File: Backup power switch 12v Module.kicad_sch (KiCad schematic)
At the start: 20 parts, among them J1 BAT IN, J2 PWR IN, J3 LOAD PWR OUT, K1 SANYOU_SRD_Form_C, Q3 BC817, U1 LM393

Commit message: DRC check
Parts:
- D7: footprint Package_TO_SOT_THT:TO-247-3_Vertical -> PCM_Package_TO_SOT_THT_AKL_OneLayer:TO-220-3_Staggered_Vertical
- K1: value SANYOU_SRD_Form_C -> SRD-12VDC-SL-C
- U1: footprint Package_SO:SOP-8_3.76x4.96mm_P1.27mm -> Package_DIP:DIP-8_W7.62mm
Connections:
- net COMMON OUT 12 +: no longer C5.1, D2.1 (K), D7.2 (K), K1.5, U1.8 (V+)
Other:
- note added: "Backup batary switch with charger, sensors and ESP controller"
- note added: "Comparator LM393"
- note added: "Switchng module"
- note removed: "Bat > PWR Signal High"
- note removed: "PWR > BAT Signal Low"
- note removed: "Pin3 < Pin2 Signal High"
- note removed: "Pin3 > Pin2 Signal High"
- note removed: "Зарядка батареи с двумя сенсорами тока"
- note removed: "Компаратор LM393"
- moved on the sheet: C5, D6, D7, J1, J2, J3, R13, R2, R3, RV1, TP1, TP2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

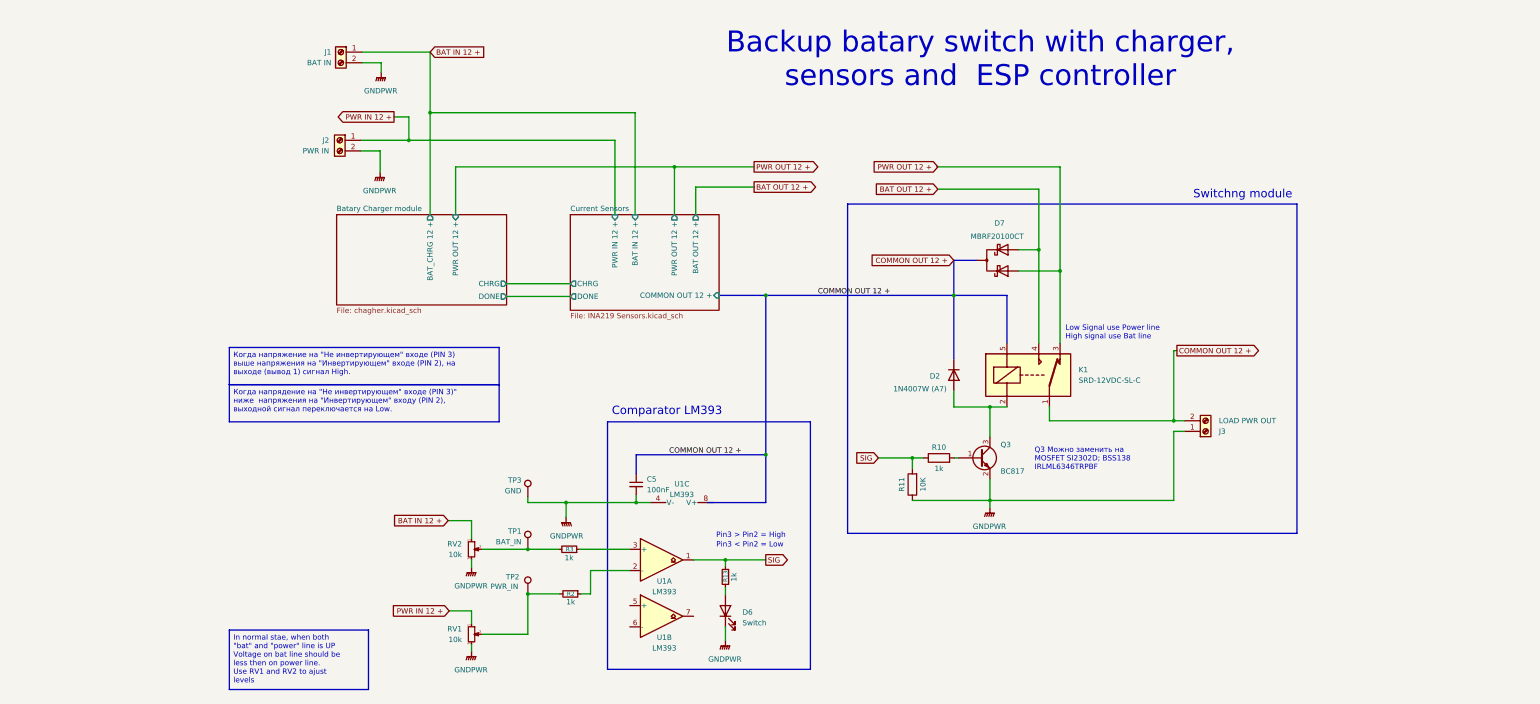
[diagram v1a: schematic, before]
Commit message: Add bat input stabilizer
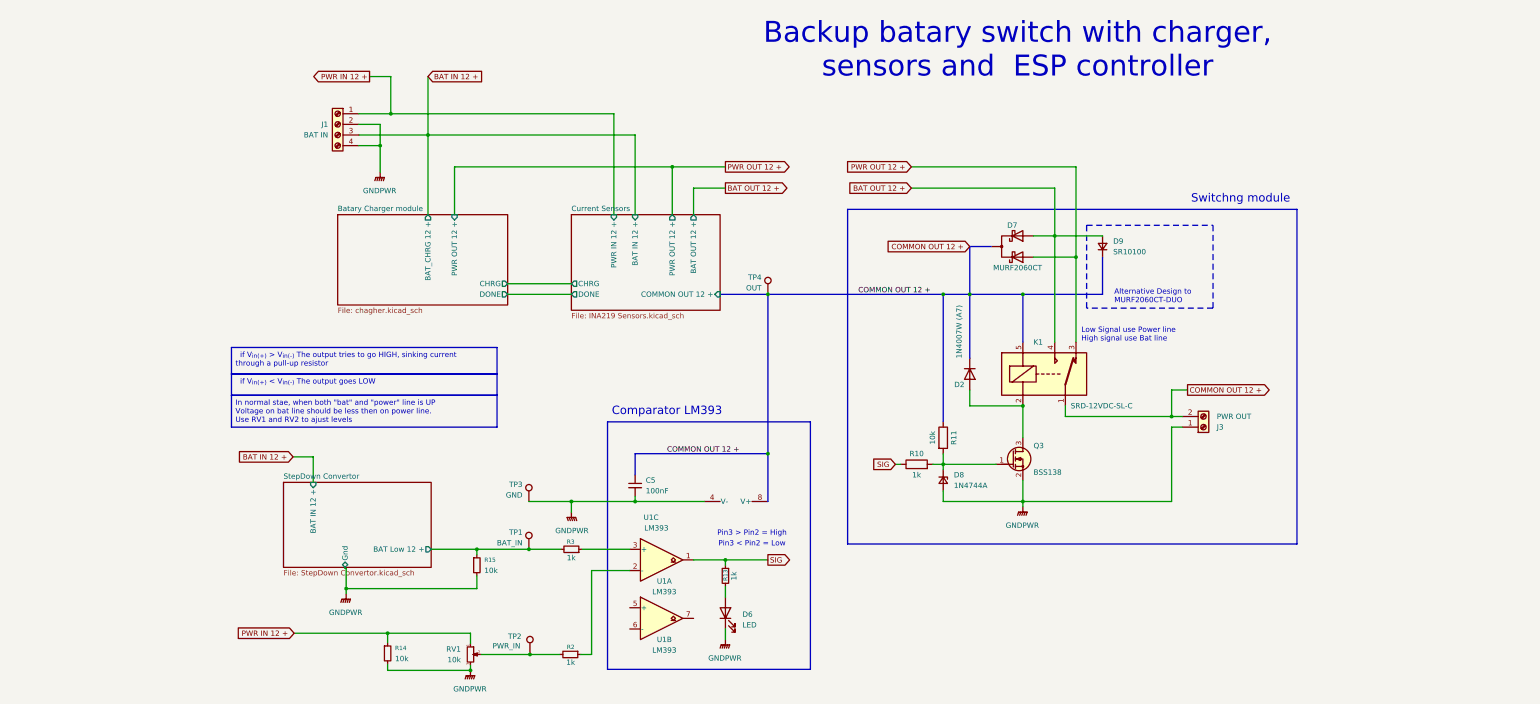
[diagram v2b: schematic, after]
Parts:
- removed J2: PWR IN, TerminalBlock_Local:ScrewTerminal_KF7.62_2P, symbol Connector:Screw_Terminal_01x02
- removed RV2: 10k, Potentiometer_THT:Potentiometer_Bourns_3296W_Vertical, symbol Device:R_Potentiometer_Small
- added D8: 1N4744A, Diode_THT:D_DO-41_SOD81_P7.62mm_Horizontal, symbol Device:D_Zener_Small
- added D9: SR10100, symbol Device:D_Small
- added R14, R15: 10k, PCM_Resistor_SMD_AKL:R_0805_2012Metric_Pad1.15x1.40mm_HandSolder, symbol Device:R_Small
- added TP4: OUT, TestPoint:TestPoint_Loop_D2.50mm_Drill1.85mm, symbol Connector:TestPoint
- D6: value Switch -> LED; descr (none) -> ON when level UP
- D7: value MBRF20100CT -> MURF2060CT
- J1: footprint TerminalBlock_Local:ScrewTerminal_KF7.62_2P -> TerminalBlock_Local:ScrewTerminal_KF7.62_4P; symbol Connector:Screw_Terminal_01x02 -> Connector:Screw_Terminal_01x04
- J3: value LOAD PWR OUT -> PWR OUT
- Q3: value BC817 -> BSS138; footprint Package_TO_SOT_SMD:SOT-23 -> PCM_Package_TO_SOT_SMD_AKL:SOT-23; symbol Transistor_BJT:BC817 -> PCM_Transistor_MOSFET_AKL:BSS138
- R11: value 10K -> 10k
- RV1: footprint Potentiometer_THT:Potentiometer_Bourns_3296W_Vertical -> PCM_Potentiometer_THT_AKL:Potentiometer_Bourns_3296W_Vertical
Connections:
- net BAT IN 12 +: now also J1.3 (Pin_3); no longer J1.1 (Pin_1)
- net BAT OUT 12 +: now also D9.2 (A)
- net GNDPWR: now also J1.4 (Pin_4), D8.2 (A), R14.2, R15.2; no longer R11.1
- net PWR IN 12 +: now also J1.1 (Pin_1), R14.1
- net SIG: no longer R11.2
- net at Q3.1 (G), R10.2: now also R11.2, D8.1 (K)
- net StepDown Convertor/BAT Low 12 +: now reaches R3.2, TP1.1
- net StepDown Convertor/BAT Low 12 +: now also R15.1
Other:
- added sheet StepDown Convertor (StepDown Convertor.kicad_sch)
- note added: "Alternative Design to MURF2060CT-DUO"
- note removed: "Q3 Можно заменить на MOSFET SI2302D; BSS138 IRLML6346TRPBF"
- moved on the sheet: D2, D6, D7, J3, K1, R10, R11, R2, R3, RV1, TP2, TP3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

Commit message: Fix comparator out signal pullup
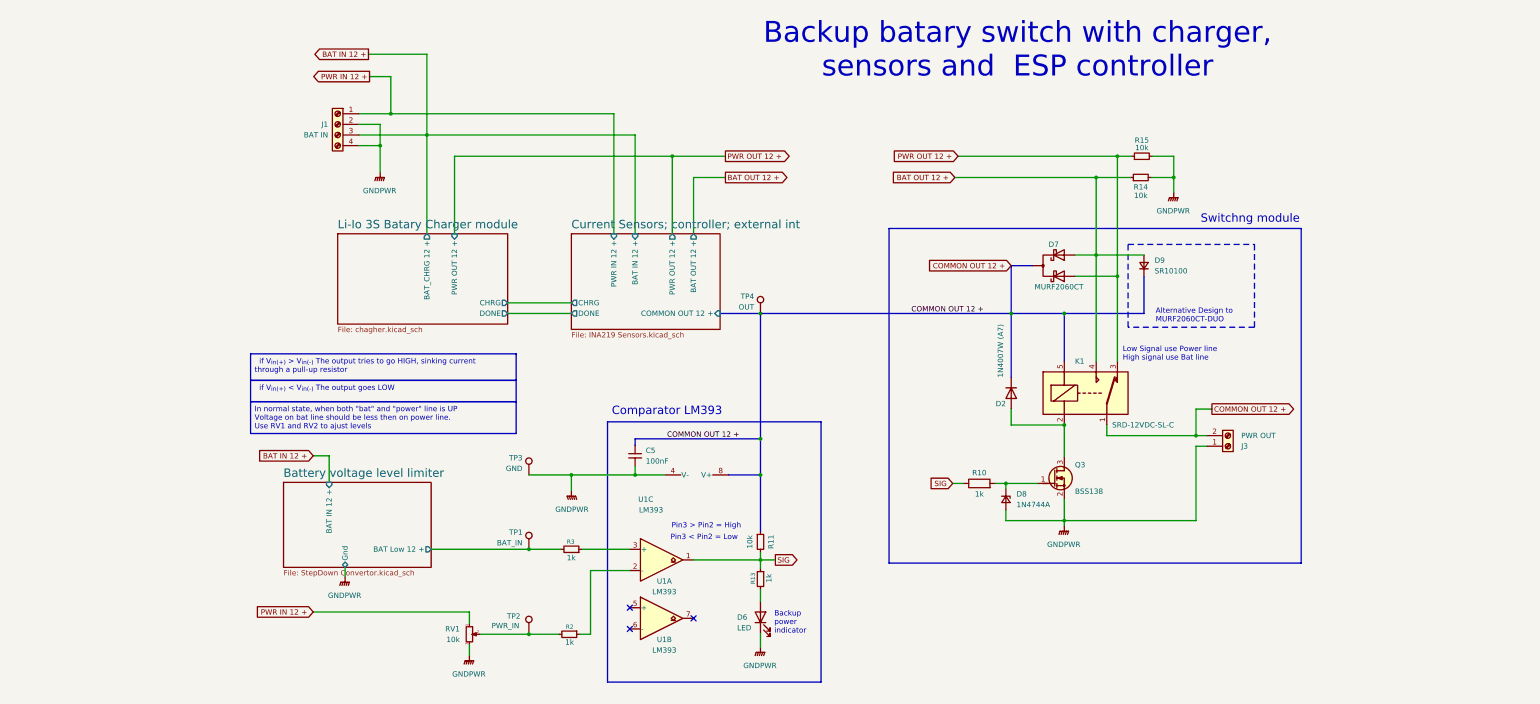
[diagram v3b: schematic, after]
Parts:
- R11: symbol Device:R -> Device:R_Small
- R14, R15: footprint PCM_Resistor_SMD_AKL:R_0805_2012Metric_Pad1.15x1.40mm_HandSolder -> Resistor_SMD:R_0805_2012Metric_Pad1.20x1.40mm_HandSolder
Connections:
- net BAT OUT 12 +: now also R14.1
- net PWR IN 12 +: no longer R14.1
- net PWR OUT 12 +: now also R15.1
- net SIG: now also R11.2
- net Battery voltage level limiter/BAT Low 12 +: no longer R15.1
- net at D8.1 (K), Q3.1 (G), R10.2: no longer R11.2
- no-connect marks 0 -> 3
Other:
- sheet Batary Charger module renamed Li-Io 3S Batary Charger module
- sheet Current Sensors renamed Current Sensors; controller; external int
- sheet StepDown Convertor renamed Battery voltage level limiter
- note added: "Backup power indicator"
- moved on the sheet: C5, D2, D6, D7, D8, D9, J3, K1, Q3, R10, R11, R13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

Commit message: Some sheme clarify
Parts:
- J1: value BAT IN -> BAT/PWR IN
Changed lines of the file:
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@@
 	(rectangle
 		(start 173.736 70.612)
-		(end 272.288 150.622)
+		(end 274.574 150.622)
 		(stroke
 			(width 0)
@@
 			)
 		)
-		(property "Value" "BAT IN"
+		(property "Value" "BAT/PWR IN"
 			(at 39.624 48.2599 0)
 			(effects
@@
 		(on_board yes)
 		(dnp no)
-		(fields_autoplaced yes)
 		(stroke
 			(width 0.1524)
@@
 		)
 		(property "Sheetname" "Current Sensors; controller; external int"
-			(at 97.79 70.8054 0)
+			(at 90.678 70.612 0)
 			(effects
 				(font
@@
 		(on_board yes)
 		(dnp no)
-		(fields_autoplaced yes)
 		(stroke
 			(width 0.1524)
@@
 		)
 		(property "Sheetname" "Li-Io 3S Batary Charger module"
-			(at 41.91 70.8054 0)
+			(at 36.068 70.358 0)
 			(effects
 				(font

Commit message: Add power sockwr
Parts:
- removed J3: PWR OUT, TerminalBlock_Local:ScrewTerminal_KF7.62_2P, symbol Connector:Screw_Terminal_01x02
- added HS1: Heatsink, Heatsink:Heatsink_Stonecold_HS-S01_13.21x6.35mm, symbol Mechanical:Heatsink
- D9: value SR10100 -> 10A10
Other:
- added sheet Power out connectors (pwr_out.kicad_sch)
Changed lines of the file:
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@@
 	)
 	(junction
-		(at 247.142 120.142)
-		(diameter 0)
-		(color 0 0 0 0)
-	)
-	(junction
 		(at 143.002 149.86)
 		(diameter 0)
@@
 		(color 0 0 0 0)
 	)
+	(junction
+		(at 233.68 120.142)
+		(diameter 0)
+		(color 0 0 0 0)
+	)
 	(no_connect
 		(at 111.76 161.29)
@@
 	(wire
 		(pts
-			(xy 247.142 122.682) (xy 249.682 122.682)
+			(xy 97.79 88.392) (xy 82.55 88.392)
 		)
 		(stroke
@@
 		)
 	)
-	(wire
+	(bus
 		(pts
-			(xy 97.79 88.392) (xy 82.55 88.392)
+			(xy 143.002 90.932) (xy 143.002 120.904)
 		)
 		(stroke
@@
 		)
 	)
-	(bus
+	(wire
 		(pts
-			(xy 143.002 90.932) (xy 143.002 120.904)
+			(xy 36.068 124.968) (xy 39.878 124.968)
 		)
 		(stroke
@@
 	(wire
 		(pts
-			(xy 36.068 124.968) (xy 39.878 124.968)
+			(xy 247.396 135.382) (xy 247.396 140.462)
 		)
 		(stroke
@@
 	(wire
 		(pts
-			(xy 247.142 120.142) (xy 249.682 120.142)
-		)
-		(stroke
-			(width 0)
-			(type default)
-		)
-	)
-	(wire
-		(pts
 			(xy 223.266 58.42) (xy 231.394 58.42)
 		)
@@
 	(wire
 		(pts
-			(xy 247.142 122.682) (xy 247.142 140.462)
-		)
-		(stroke
-			(width 0)
-			(type default)
-		)
-	)
-	(wire
-		(pts
 			(xy 218.186 76.962) (xy 223.266 76.962)
 		)
@@
 		)
 	)
-	(wire
-		(pts
-			(xy 215.646 140.462) (xy 247.142 140.462)
-		)
-		(stroke
-			(width 0)
-			(type default)
-		)
-	)
 	(bus
 		(pts
@@
 	(wire
 		(pts
-			(xy 247.142 113.792) (xy 247.142 120.142)
+			(xy 233.68 108.966) (xy 233.68 120.142)
 		)
 		(stroke
@@
 		)
 	)
+	(wire
+		(pts
+			(xy 233.68 120.142) (xy 236.474 120.142)
+		)
+		(stroke
+			(width 0)
+			(type default)
+		)
+	)
 	(bus
 		(pts
@@
 	(wire
 		(pts
-			(xy 225.806 120.142) (xy 247.142 120.142)
+			(xy 225.806 120.142) (xy 233.68 120.142)
 		)
 		(stroke
@@
 	(wire
 		(pts
-			(xy 107.95 43.18) (xy 107.95 71.882)
+			(xy 247.396 140.462) (xy 215.646 140.462)
 		)
 		(stroke
@@
 	(wire
 		(pts
-			(xy 127 58.42) (xy 127 71.882)
+			(xy 107.95 43.18) (xy 107.95 71.882)
 		)
 		(stroke
@@
 	(wire
 		(pts
-			(xy 215.646 135.382) (xy 215.646 140.462)
+			(xy 127 58.42) (xy 127 71.882)
 		)
 		(stroke
@@
 	(wire
 		(pts
-			(xy 247.142 113.792) (xy 250.952 113.792)
+			(xy 233.68 108.966) (xy 251.46 108.966)
+		)
+		(stroke
+			(width 0)
+			(type default)
+		)
+	)
+	(wire
+		(pts
+			(xy 215.646 135.382) (xy 215.646 140.462)
 		)
 		(stroke
@@
 	(global_label "COMMON OUT 12 +"
 		(shape output)
-		(at 250.952 113.792 0)
+		(at 251.46 108.966 0)
 		(fields_autoplaced yes)
 		(effects
@@
 		)
 		(property "Intersheetrefs" "${INTERSHEET_REFS}"
-			(at 272.6243 113.792 0)
+			(at 273.1323 108.966 0)
 			(effects
 				(font
@@
 		(property "Intersheetrefs" "${INTERSHEET_REFS}"
 			(at 181.2737 79.502 0)
+			(show_name yes)
 			(effects
 				(font
@@
 		(fields_autoplaced yes)
 		(property "Reference" "D9"
-			(at 237.236 78.2319 90)
+			(at 237.49 78.2319 90)
 			(effects
 				(font
@@
 			)
 		)
-		(property "Value" "SR10100"
-			(at 237.236 80.7719 90)
+		(property "Value" "10A10"
+			(at 237.49 80.7719 90)
 			(effects
 				(font
@@
 	)
 	(symbol
+		(lib_id "Mechanical:Heatsink")
+		(at 209.55 79.502 90)
+		(unit 1)
+		(exclude_from_sim no)
+		(in_bom yes)
+		(on_board yes)
+		(dnp no)
+		(fields_autoplaced yes)
+		(property "Reference" "HS1"
+			(at 210.82 78.2446 90)
+			(effects
+				(font
+					(size 1.27 1.27)
+				)
+				(justify right)
+				(hide yes)
+			)
+		)
+		(property "Value" "Heatsink"
+			(at 210.82 80.7846 90)
+			(effects
+				(font
+					(size 1.27 1.27)
+				)
+				(justify right)
+				(hide yes)
+			)
+		)
+		(property "Footprint" "Heatsink:Heatsink_Stonecold_HS-S01_13.21x6.35mm"
+			(at 209.55 79.1972 0)
+			(effects
+				(font
+					(size 1.27 1.27)
+				)
+				(hide yes)
+			)
+		)
+		(property "Datasheet" "~"
+			(at 209.55 79.1972 0)
+			(effects
+				(font
+					(size 1.27 1.27)
+				)
+				(hide yes)
+			)
+		)
+		(property "Description" "Heatsink"
+			(at 209.55 79.502 0)
+			(effects
+				(font
+					(size 1.27 1.27)
+				)
+				(hide yes)
+			)
+		)
+		(property "descr" ""
+			(at 209.55 79.502 0)
+			(effects
+				(font
+					(size 1.27 1.27)
+				)
+				(hide yes)
+			)
+		)
+		(instances
+			(project ""
+				(path "/7ca50d0f-f559-49b7-8c40-8a0dd824c105"
+					(reference "HS1")
+					(unit 1)
+				)
+			)
+		)
+	)
+	(symbol
 		(lib_id "Connector:TestPoint")
 		(at 87.63 129.54 0)
@@
 		)
 		(property "Value" "GNDPWR"
-			(at 97.917 137.795 0)
+			(at 97.917 137.16 0)
 			(effects
 				(font
@@
 	)
 	(symbol
-		(lib_id "Connector:Screw_Terminal_01x02")
-		(at 254.762 122.682 0)
-		(mirror x)
-		(unit 1)
-		(exclude_from_sim no)
-		(in_bom yes)
-		(on_board yes)
-		(dnp no)
-		(property "Reference" "J3"
-			(at 257.937 122.6821 0)
-			(effects
-				(font
-					(size 1.27 1.27)
-				)
-				(justify left)
-			)
-		)
-		(property "Value" "PWR OUT"
-			(at 257.937 120.1421 0)
-			(effects
-				(font
-					(size 1.27 1.27)
-				)
-				(justify left)
-			)
-		)
-		(property "Footprint" "TerminalBlock_Local:ScrewTerminal_KF7.62_2P"
-			(at 254.762 122.682 0)
-			(effects
-				(font
-					(size 1.27 1.27)
-				)
-				(hide yes)
-			)
-		)
-		(property "Datasheet" "~"
-			(at 254.762 122.682 0)
-			(effects
-				(font
-					(size 1.27 1.27)
-				)
-				(hide yes)
-			)
-		)
-		(property "Description" "Generic screw terminal, single row, 01x02, script generated (kicad-library-utils/schlib/autogen/connector/)"
-			(at 254.762 122.682 0)
-			(effects
-				(font
-					(size 1.27 1.27)
-				)
-				(hide yes)
-			)
-		)
-		(property "descr" ""
-			(at 254.762 122.682 0)
-			(effects
-				(font
-					(size 1.27 1.27)
-				)
-			)
-		)
-		(pin "1"
-		)
-		(pin "2"
-		)
-		(instances
-			(project ""
-				(path "/7ca50d0f-f559-49b7-8c40-8a0dd824c105"
-					(reference "J3")
-					(unit 1)
-				)
-			)
-		)
-	)
-	(symbol
 		(lib_id "Connector:TestPoint")
 		(at 87.63 167.386 0)
@@
 		)
 		(property "Value" "SRD-12VDC-SL-C"
-			(at 227.076 117.602 0)
+			(at 205.74 120.65 0)
 			(effects
 				(font
@@
 				)
 			)
+		)
+	)
+	(sheet
+		(at 236.474 115.062)
+		(size 33.528 20.32)
+		(exclude_from_sim no)
+		(in_bom yes)
+		(on_board yes)
+		(dnp no)
+		(stroke
+			(width 0.1524)
+			(type solid)
+		)
+		(fill
+			(color 249 253 255 1.0000)
+		)
+		(property "Sheetname" "Power out connectors"
+			(at 249.936 114.3 0)
+			(effects
+				(font
+					(size 1.27 1.27)
+				)
+				(justify left bottom)
+			)
+		)
+		(property "Sheetfile" "pwr_out.kicad_sch"
+			(at 236.474 135.9666 0)
+			(effects
+				(font
+					(size 1.27 1.27)
+				)
+				(justify left top)
+			)
+		)
+		(pin "GND" input
+			(at 247.396 135.382 270)
+			(effects
+				(font
+					(size 1.27 1.27)
+				)
+				(justify left)
+			)
+		)
+		(pin "COMMON OUT 12 +" input
+			(at 236.474 120.142 180)
+			(effects
+				(font
+					(size 1.27 1.27)
+				)
+				(justify left)
+			)
+		)
+		(instances
+			(project "Backup power switch 12v Module"
+				(path "/7ca50d0f-f559-49b7-8c40-8a0dd824c105"
+					(page "5")
+				)
+			)
